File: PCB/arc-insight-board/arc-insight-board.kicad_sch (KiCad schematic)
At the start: 39 parts, among them J1 USB_C_Receptacle, J2 Conn_01x06, J3 Conn_01x05, J4 Conn_01x02, J5 Conn_01x02, J6 FPC_24PIN, J7 Conn_01x02, J8 U.FL, M1 Electret, U1 ESP32-S3, U2 MAX98357A, U3 MAX98357A, U4 TP4054, U5 Comparator, U6 ME6211C33M5, Y1 40MHz

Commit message: Add cap-touch firmware and TOUCH routing; refresh production outputs
- Firmware: cap-touch reading on GPIO1 (touch.cpp/h), threshold 80, 900ms hold
- PCB: route /TOUCH pad to ESP32; update schematic/project files
- Regenerate gerbers (incl. /TOUCH net), drill files, positions.csv, BOM, gerbers.zip
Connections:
- net TOUCH: now reaches U1.6 (GPIO1)
- no-connect marks 38 -> 37
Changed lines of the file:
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@@
-	)
-	(no_connect
-		(at 116.84 68.58)
 	)
 	(no_connect
@@
 		(pts
 			(xy 139.7 50.8) (xy 139.7 58.42)
+		)
+		(stroke
+			(width 0)
+			(type default)
+		)
+	)
+	(wire
+		(pts
+			(xy 104.14 68.58) (xy 116.84 68.58)
 		)
 		(stroke
@@
 		(effects
 			(font
+				(size 1.27 1.27)
+			)
+			(justify left bottom)
+		)
+	)
+	(label "TOUCH"
+		(at 104.14 68.58 0)
+		(effects
+			(font

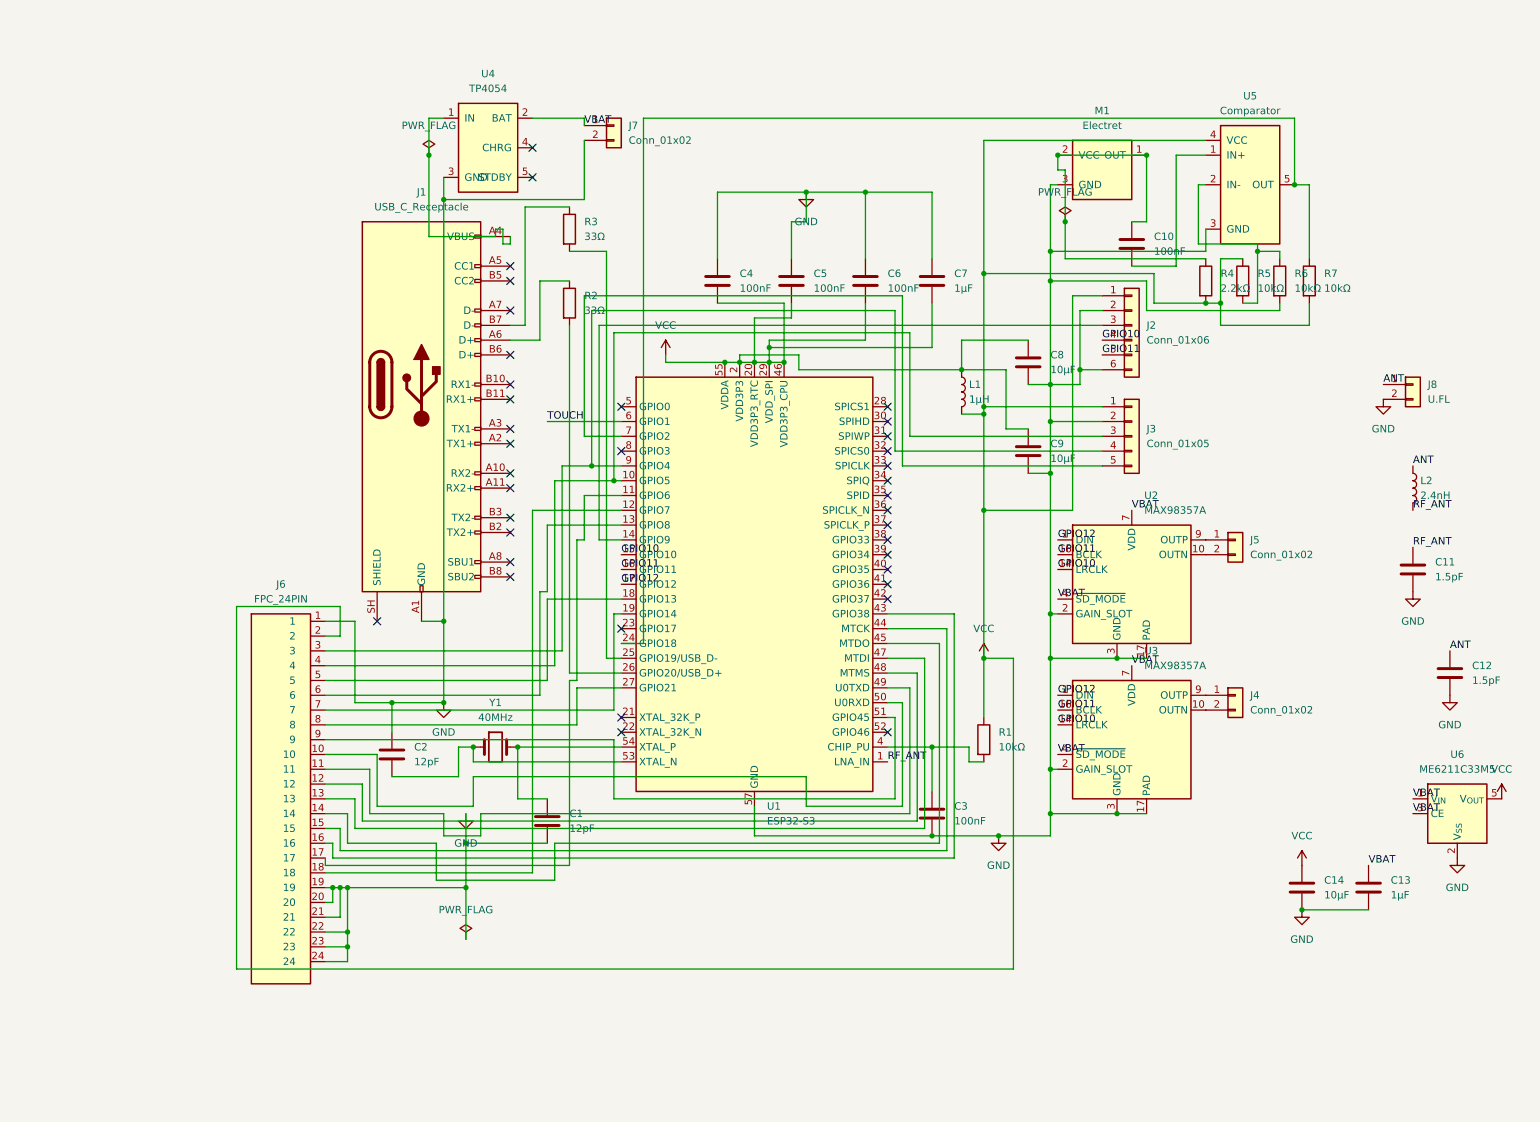
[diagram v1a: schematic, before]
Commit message: Rewrite schematic to label-based net connectivity matching PCB
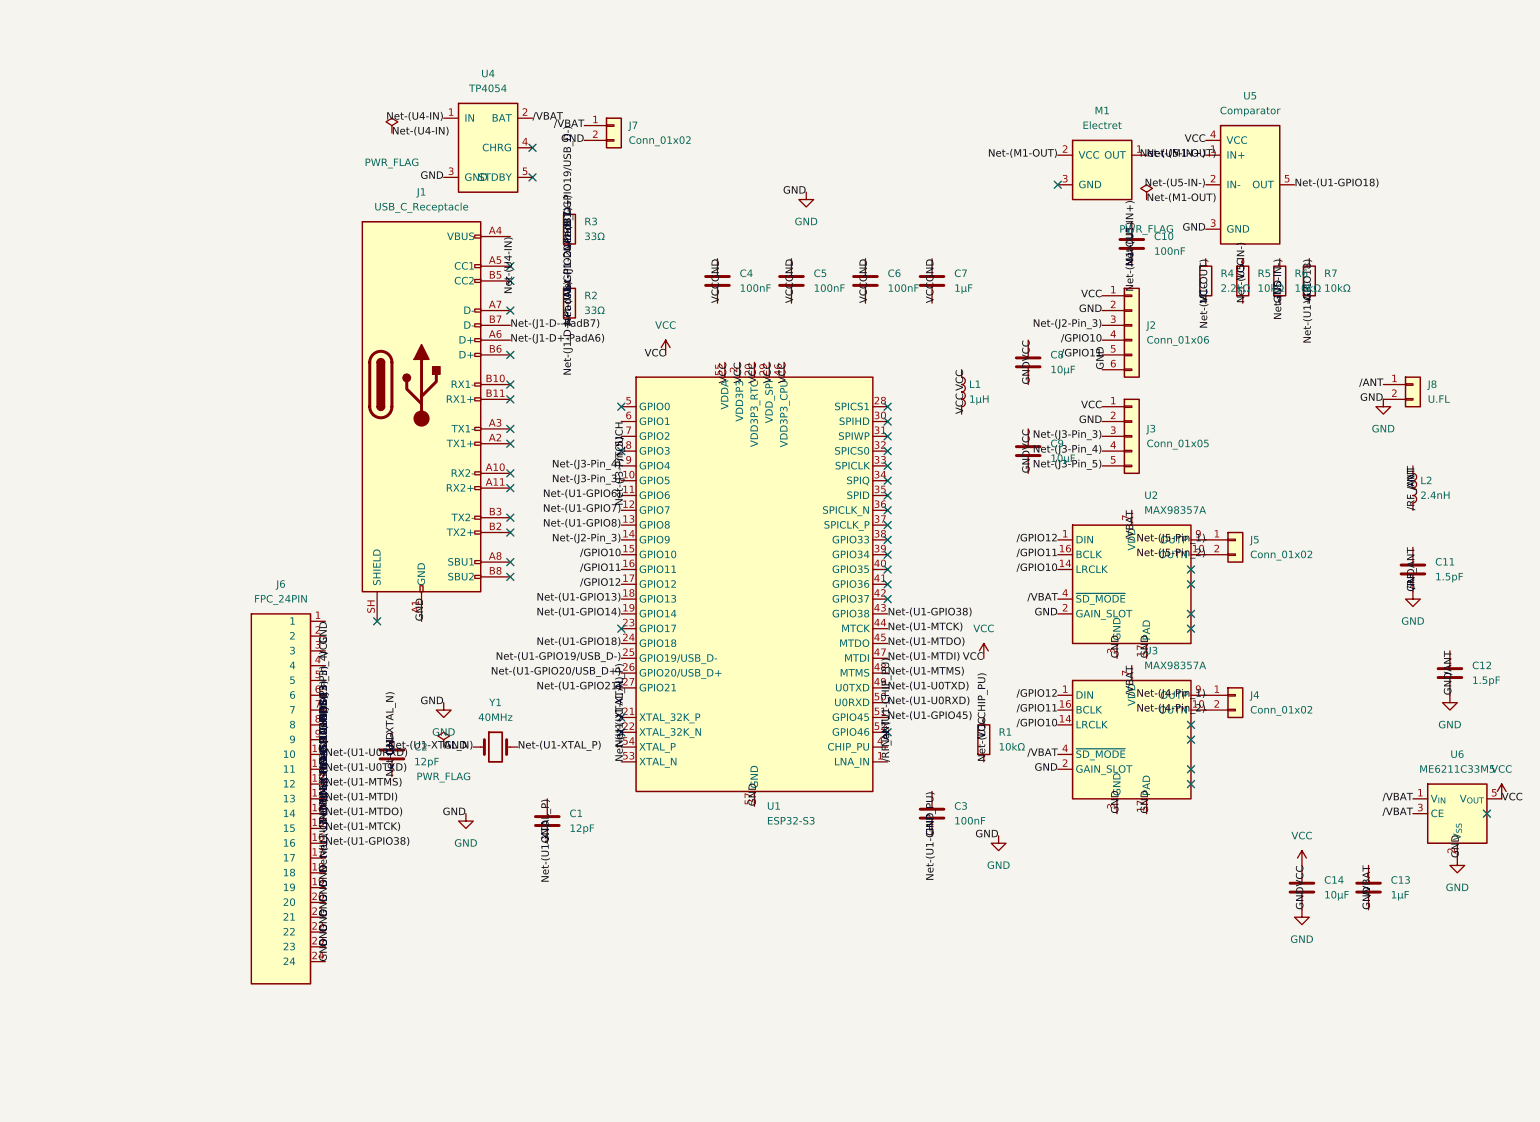
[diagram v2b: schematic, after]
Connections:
- net GND: no longer M1.3 (GND)
- net Net-(M1-OUT): now reaches C10.1, M1.1 (OUT), M1.2 (VCC), R4.1
- net Net-(U5-IN+): now reaches C10.2, U5.1 (IN+)
- net Net-(U5-IN-): now reaches R5.2, R6.1, U5.2 (IN-)
- net Net-(U1-XTAL_N): now reaches C2.2, U1.53 (XTAL_N), Y1.1
- net Net-(U1-XTAL_P): now reaches C1.1, U1.54 (XTAL_P), Y1.2
- net Net-(J3-Pin_3): now reaches J3.3 (Pin_3), J6.4, U1.10 (GPIO5)
- net Net-(U1-GPIO6): now reaches J6.17, U1.11 (GPIO6)
- net Net-(U1-GPIO7): now reaches J6.18, U1.12 (GPIO7)
- net Net-(U1-GPIO8): now reaches J6.6, U1.13 (GPIO8)
- net Net-(J2-Pin_3): now reaches J2.3 (Pin_3), U1.14 (GPIO9)
- net Net-(U1-GPIO13): now reaches J6.5, U1.18 (GPIO13)
- net Net-(U1-GPIO14): now reaches J6.7, U1.19 (GPIO14)
- net Net-(U1-GPIO18): now reaches R7.1, U1.24 (GPIO18), U5.5 (OUT)
- net Net-(U1-GPIO19/USB_D-): now reaches R3.2, U1.25 (GPIO19/USB_D-)
- net Net-(U1-GPIO20/USB_D+): now reaches R2.2, U1.26 (GPIO20/USB_D+)
- net Net-(U1-GPIO21): now reaches J6.8, U1.27 (GPIO21)
- net Net-(U1-CHIP_PU): now reaches C3.1, R1.2, U1.4 (CHIP_PU)
- net Net-(U1-GPIO38): now reaches J6.16, U1.43 (GPIO38)
- net Net-(U1-MTCK): now reaches J6.15, U1.44 (MTCK)
- net Net-(U1-MTDO): now reaches J6.14, U1.45 (MTDO)
- net Net-(U1-MTDI): now reaches J6.13, U1.47 (MTDI)
- net Net-(U1-MTMS): now reaches J6.12, U1.48 (MTMS)
- net Net-(U1-U0TXD): now reaches J6.11, U1.49 (U0TXD)
- net Net-(U1-U0RXD): now reaches J6.10, U1.50 (U0RXD)
- net Net-(U1-GPIO45): now reaches J6.9, U1.51 (GPIO45)
- net Net-(J3-Pin_5): now reaches J3.5 (Pin_5), U1.7 (GPIO2)
- net Net-(J3-Pin_4): now reaches J3.4 (Pin_4), J6.3, U1.9 (GPIO4)
- net Net-(U4-IN): now reaches J1.A4 (VBUS), J1.A9 (VBUS), J1.B4 (VBUS), J1.B9 (VBUS), U4.1 (IN)
- net Net-(J1-D+-PadA6): now reaches J1.A6 (D+), R2.1
- net Net-(J4-Pin_2): now reaches J4.2 (Pin_2), U3.10 (OUTN)
- net Net-(J4-Pin_1): now reaches J4.1 (Pin_1), U3.9 (OUTP)
- net Net-(J5-Pin_1): now reaches J5.1 (Pin_1), U2.9 (OUTP)
- net Net-(J5-Pin_2): now reaches J5.2 (Pin_2), U2.10 (OUTN)
- net Net-(J1-D--PadB7): now reaches J1.B7 (D-), R3.1
- net ANT renamed /ANT
- net GPIO10 renamed /GPIO10
- net GPIO11 renamed /GPIO11
- net GPIO12 renamed /GPIO12
- net RF_ANT renamed /RF_ANT
- net TOUCH renamed /TOUCH
- net VBAT renamed /VBAT
- no-connect marks 37 -> 47

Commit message: Rewrite schematic with wired layout, CC pulldowns, grounded shield, drop L1
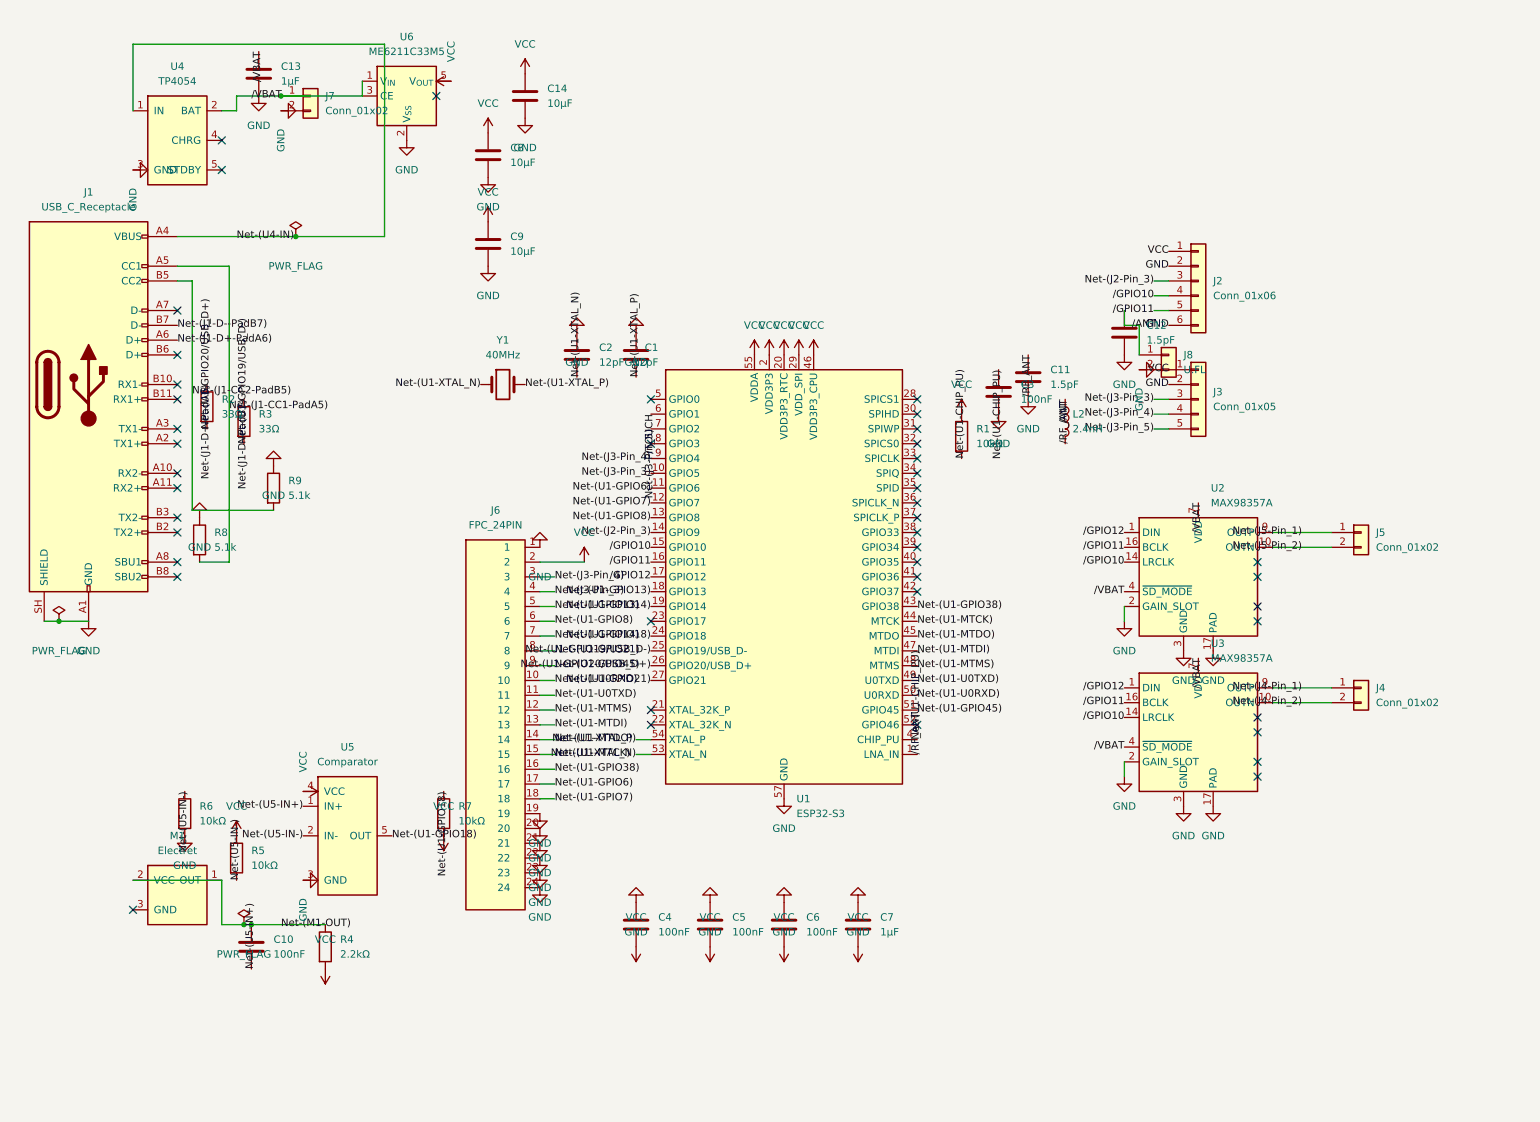
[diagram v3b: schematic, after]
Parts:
- removed L1: 1µH, Inductor_SMD:L_0603_1608Metric, symbol Device:L
- added R8, R9: 5.1k, Resistor_SMD:R_0402_1005Metric, symbol Device:R
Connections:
- net GND: now also J1.SH (SHIELD), R8.1, R9.1
- net Net-(J1-CC1-PadA5): now reaches J1.A5 (CC1)
- net Net-(J1-CC1-PadA5): now also R8.2
- net Net-(J1-CC2-PadB5): now reaches J1.B5 (CC2)
- net Net-(J1-CC2-PadB5): now also R9.2
- no-connect marks 47 -> 44
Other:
- moved on the sheet: C1, C10, C11, C12, C13, C14, C2, C3, C4, C5, C6, C7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

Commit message: Update PCB: add R8/R9 CC pulldowns, ground USB-C shield
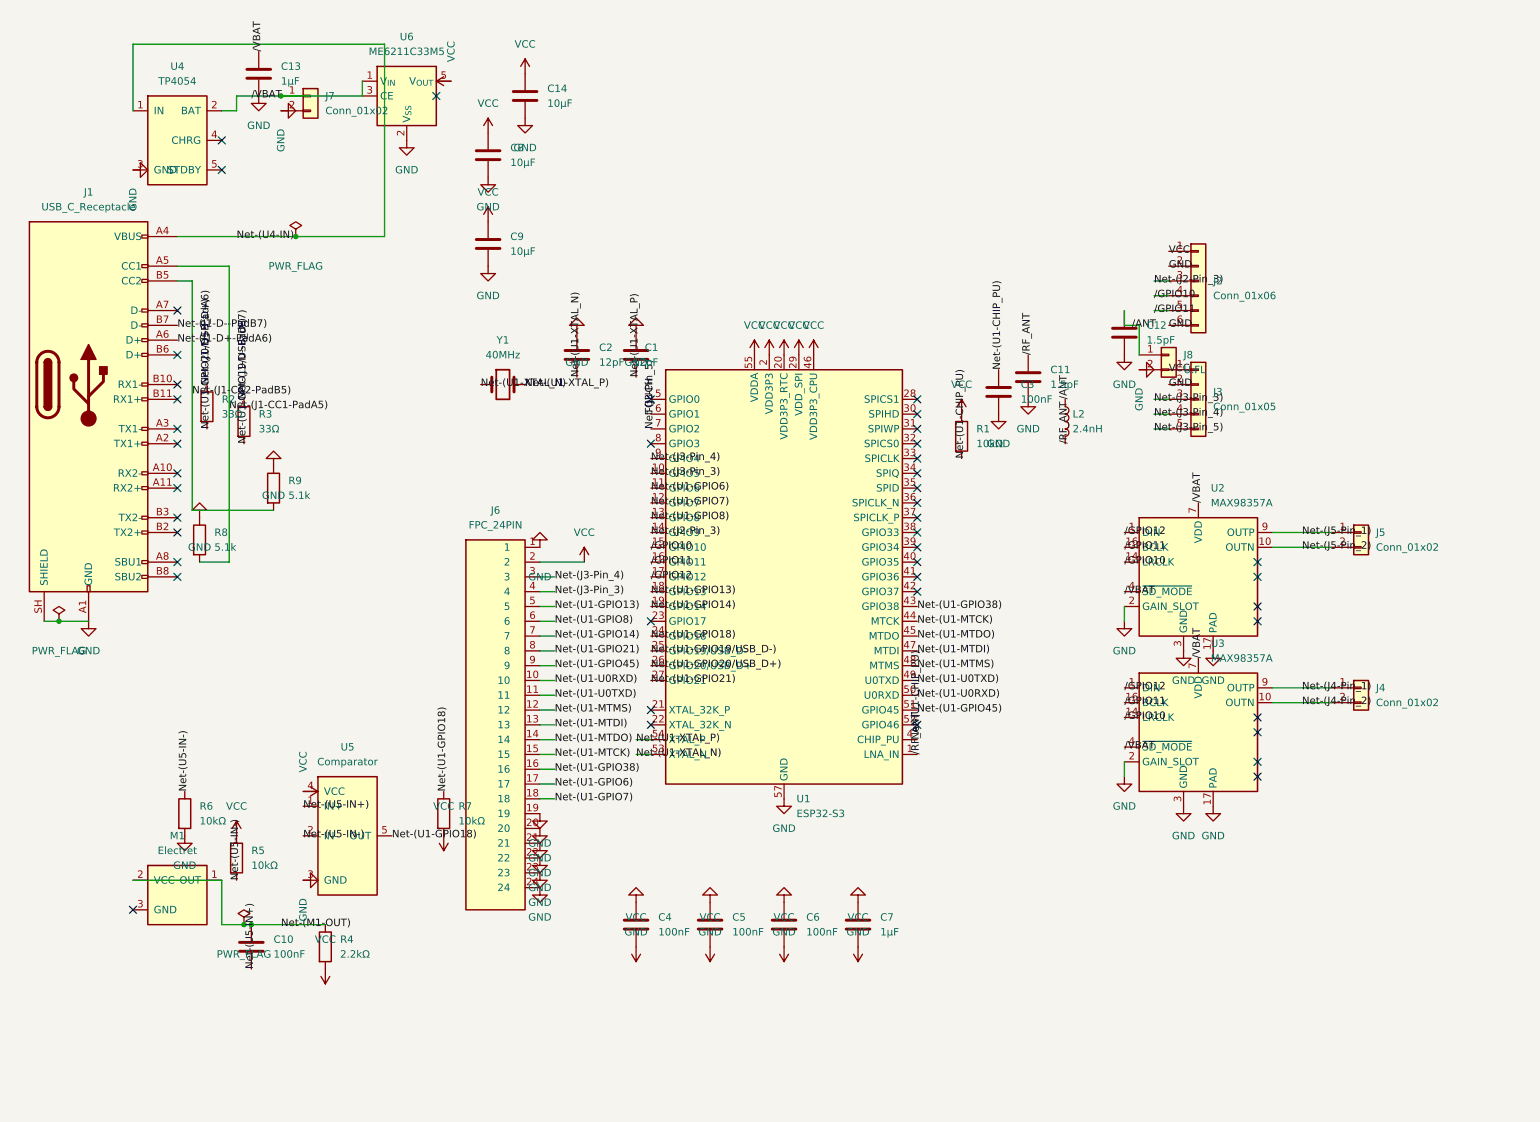
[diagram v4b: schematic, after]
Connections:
- net /TOUCH renamed TOUCH

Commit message: Edited files
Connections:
- net GND: now also R8.2; no longer R8.1
- net Net-(J1-CC1-PadA5): no longer names the net of J1.A5 (CC1)
- net Net-(J1-CC1-PadA5): now also R8.1; no longer R8.2
- net Net-(J1-CC2-PadB5): no longer names the net of J1.B5 (CC2), R9.2
- net Net-(J1-D+-PadA6): no longer names the net of J1.A6 (D+), R2.1
- net Net-(J1-D--PadB7): no longer names the net of J1.B7 (D-)
- net Net-(J1-D--PadB7): now also R3.2; no longer R3.1
- net Net-(J2-Pin_3) renamed Net-J2Pin_3
- net Net-(J3-Pin_3) renamed Net-J3Pin_3
- net Net-(J3-Pin_4) renamed Net-J3Pin_4
- net Net-(J3-Pin_5) renamed Net-J3Pin_5
- net Net-(J4-Pin_1): no longer names the net of J4.1 (Pin_1), U3.9 (OUTP)
- net Net-(J4-Pin_2): no longer names the net of J4.2 (Pin_2), U3.10 (OUTN)
- net Net-(J5-Pin_1): no longer names the net of J5.1 (Pin_1), U2.9 (OUTP)
- net Net-(J5-Pin_2): no longer names the net of J5.2 (Pin_2), U2.10 (OUTN)
- net Net-(U1-CHIP_PU) renamed Net-CHIP_PU
- net Net-(U1-GPIO13) renamed Net-GPIO13
- net Net-(U1-GPIO14) renamed Net-GPIO14
- net Net-(U1-GPIO18) renamed Net-GPIO18
- net Net-(U1-GPIO19/USB_D-) renamed Net-GPIO19
- net Net-GPIO19: now also R3.1; no longer R3.2
- net Net-(U1-GPIO20/USB_D+) renamed Net-GPIO20
- net Net-(U1-GPIO21) renamed Net-GPIO21
- net Net-(U1-GPIO38) renamed Net-GPIO38
- net Net-(U1-GPIO45) renamed Net-GPIO45
- net Net-(U1-GPIO6) renamed Net-GPIO6
- net Net-(U1-GPIO7) renamed Net-GPIO7
- net Net-(U1-GPIO8) renamed Net-GPIO8
- net Net-(U1-MTCK) renamed Net-MTCK
- net Net-(U1-MTDI) renamed Net-MTDI
- net Net-(U1-MTDO) renamed Net-MTDO
- net Net-(U1-MTMS) renamed Net-MTMS
- net Net-(U1-U0RXD) renamed Net-U0RXD
- net Net-(U1-U0TXD) renamed Net-U0TXD
- net Net-(U1-XTAL_N) renamed Net-XTAL_N
- net Net-XTAL_N: now also Y1.2; no longer Y1.1
- net Net-(U1-XTAL_P) renamed Net-XTAL_P
- net Net-XTAL_P: now also Y1.1; no longer Y1.2
- net Net-(U4-IN): no longer names the net of J1.A4 (VBUS), J1.A9 (VBUS), J1.B4 (VBUS), J1.B9 (VBUS), U4.1 (IN)
- net Net-(U5-IN+) renamed Net-IN+
- net Net-(U5-IN-) renamed Net-IN-
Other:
- moved on the sheet: C1, C10, C11, C12, C13, C14, C2, C3, C8, J2, J3, J4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
